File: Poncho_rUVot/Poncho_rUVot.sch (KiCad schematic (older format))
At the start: 20 parts, among them J1 Screw_Terminal_01x03, K1 SANYOU_SRD_Form_C, P1 Conn_01x03, P2 Conn_01x03, P3 Conn_01x04, P4 Conn_01x03, P5 Conn_01x02, P6 Conn_01x02, P7 Conn_01x06, P8 Conn_01x04, P9 Conn_01x08, Q1 BC548, Q2 BC548

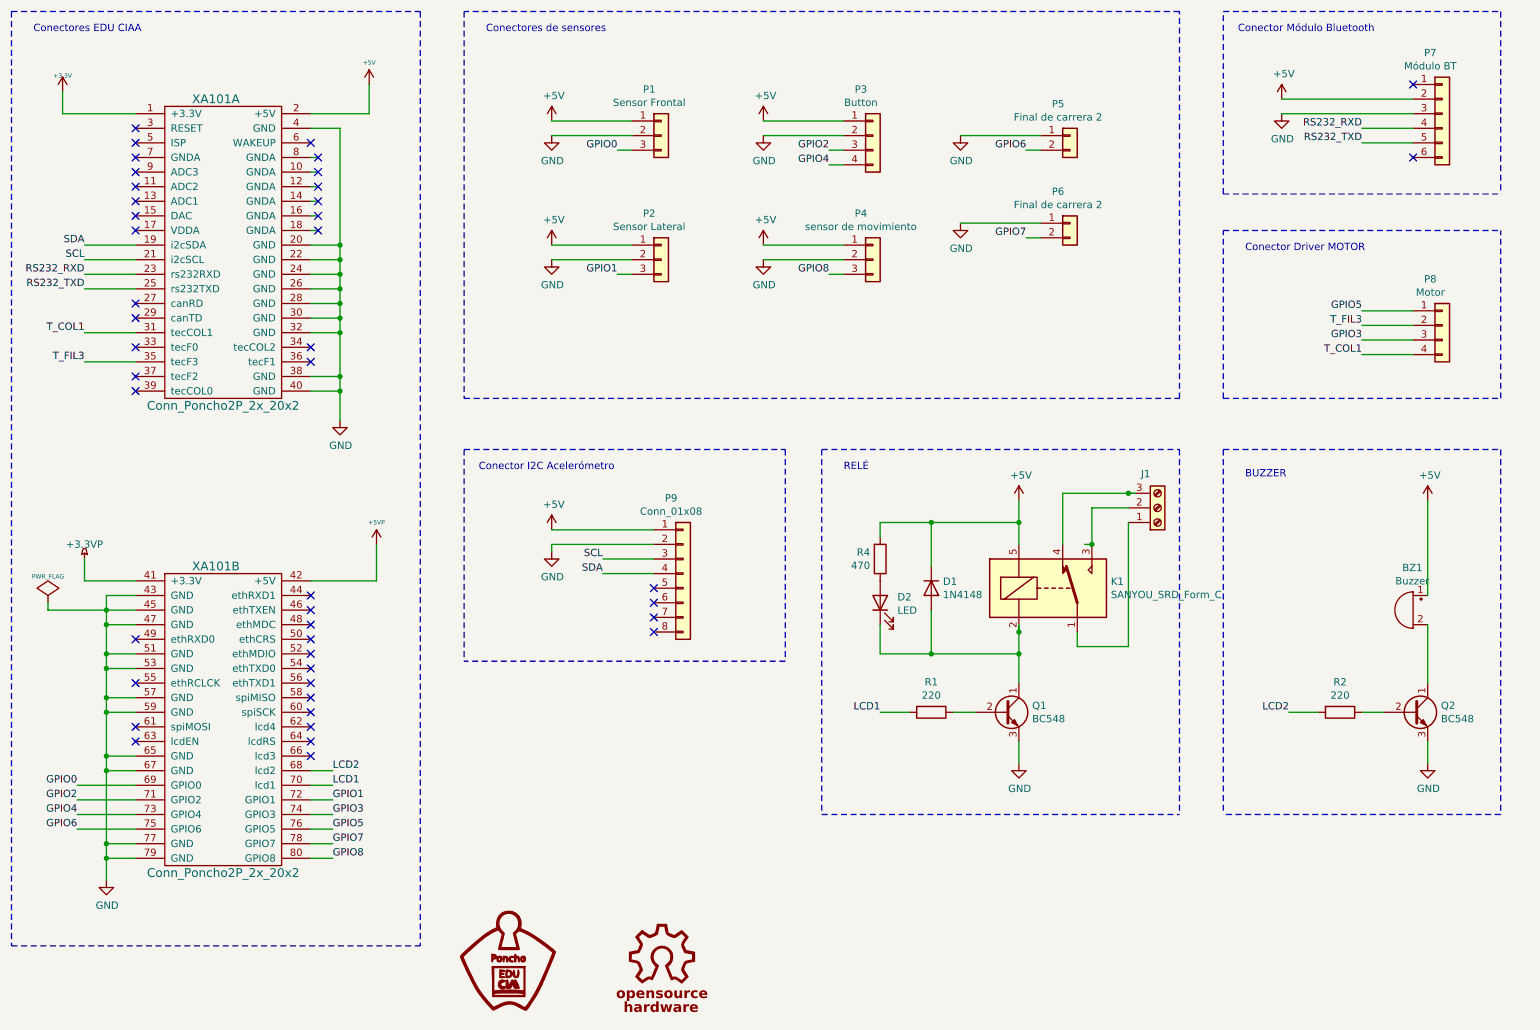
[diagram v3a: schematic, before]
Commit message: Se agrega el PCB
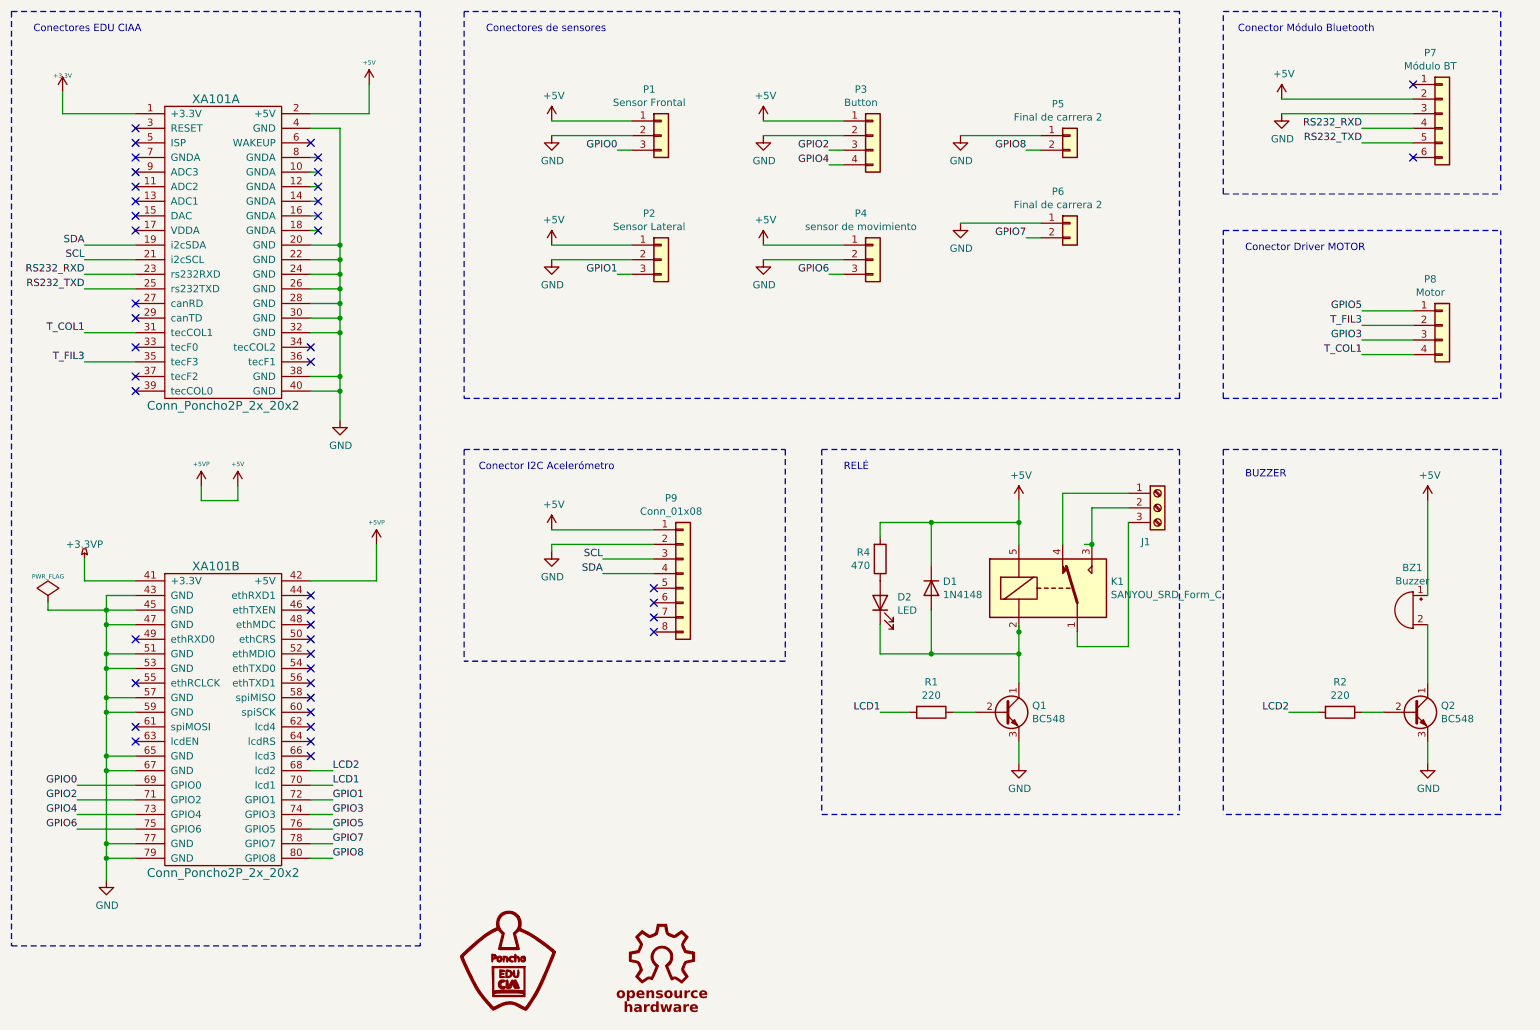
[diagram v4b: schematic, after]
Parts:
- P8: footprint Connector_PinHeader_2.54mm:PinHeader_1x04_P2.54mm_Horizontal -> Connector_PinHeader_2.54mm:PinHeader_1x04_P2.54mm_Vertical
- Q1, Q2: footprint Package_TO_SOT_THT:TO-92_Inline -> Package_TO_SOT_THT:TO-92L
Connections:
- net +5VP is gone; now on net +5V: XA101.42 (+5V)
- net GPIO6: now also P4.3 (Pin_3); no longer P5.2 (Pin_2)
- net GPIO8: now also P5.2 (Pin_2); no longer P4.3 (Pin_3)
- net at J1.1 (Pin_1): now also K1.4; no longer K1.1
- net at J1.3 (Pin_3): now also K1.1; no longer K1.4
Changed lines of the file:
@@
 F 0 "P8" H 10468 3217 50  0000 C CNN
 F 1 "Conn_01x04" H 10468 3126 50  0001 C CNN
-F 2 "Connector_PinHeader_2.54mm:PinHeader_1x04_P2.54mm_Horizontal" H 10550 2900 50  0001 C CNN
+F 2 "Connector_PinHeader_2.54mm:PinHeader_1x04_P2.54mm_Vertical" H 10550 2900 50  0001 C CNN
 F 3 "~" H 10550 2900 50  0001 C CNN
 F 4 "Motor" H 10468 3126 50  0000 C CNN "Field4"
@@
 F 0 "Q2" H 10541 5596 50  0000 L CNN
 F 1 "BC548" H 10541 5505 50  0000 L CNN
-F 2 "Package_TO_SOT_THT:TO-92_Inline" H 10550 5475 50  0001 L CIN
+F 2 "Package_TO_SOT_THT:TO-92L" H 10550 5475 50  0001 L CIN
 F 3 "https://www.onsemi.com/pub/Collateral/BC550-D.pdf" H 10350 5550 50  0001 L CNN
 	1    10350 5550
@@
 Conector Driver MOTOR
 $Comp
-L Poncho_rUVot-rescue:Screw_Terminal_01x03-Connector-conectores-rescue J1
-U 1 1 606412BA
-P 8600 4150
-F 0 "J1" H 8518 3917 50  0000 C CNN
-F 1 "Screw_Terminal_01x03" H 8518 3916 50  0001 C CNN
-F 2 "TerminalBlock_Phoenix:TerminalBlock_Phoenix_MKDS-1,5-3-5.08_1x03_P5.08mm_Horizontal" H 8600 4150 50  0001 C CNN
-F 3 "~" H 8600 4150 50  0001 C CNN
-	1    8600 4150
-	1    0    0    1
-$EndComp
-Wire Wire Line
-	7950 4050 8400 4050
-Connection ~ 8400 4050
-Wire Wire Line
-	8400 4050 8450 4050
-$Comp
 L Poncho_rUVot-rescue:1N4148-Diode-conectores-rescue D1
 U 1 1 60659DD3
@@
 F 0 "Q1" H 7741 5596 50  0000 L CNN
 F 1 "BC548" H 7741 5505 50  0000 L CNN
-F 2 "Package_TO_SOT_THT:TO-92_Inline" H 7750 5475 50  0001 L CIN
+F 2 "Package_TO_SOT_THT:TO-92L" H 7750 5475 50  0001 L CIN
 F 3 "https://www.onsemi.com/pub/Collateral/BC550-D.pdf" H 7550 5550 50  0001 L CNN
 	1    7550 5550
@@
 	5900 2450 6450 2450
 Text Label 6350 2550 2    50   ~ 0
-GPIO8
+GPIO6
 Wire Wire Line
 	6350 2550 6450 2550
@@
 	7700 1700 7800 1700
 Text Label 7700 1700 2    50   ~ 0
-GPIO6
+GPIO8
 $Comp
 L Poncho_rUVot-rescue:Conn_01x03-Connector_Generic-conectores-rescue P1
@@
 EndData
 $EndBitmap
+$Comp
+L Poncho_rUVot-rescue:+5V #PWR0118
+U 1 1 6080CF4B
+P 2300 4000
+F 0 "#PWR0118" H 2300 4090 20  0001 C CNN
+F 1 "+5V" H 2300 4150 30  0000 C CNN
+F 2 "" H 2300 4000 60  0000 C CNN
+F 3 "" H 2300 4000 60  0000 C CNN
+	1    2300 4000
+	1    0    0    -1
+$EndComp
+$Comp
+L Poncho_rUVot-rescue:+5VP #PWR0119
+U 1 1 608141D3
+P 2050 4000
+F 0 "#PWR0119" H 2050 4090 20  0001 C CNN
+F 1 "+5VP" H 2050 4150 30  0000 C CNN
+F 2 "" H 2050 4000 60  0000 C CNN
+F 3 "" H 2050 4000 60  0000 C CNN
+	1    2050 4000
+	1    0    0    -1
+$EndComp
+Wire Wire Line
+	2050 4000 2050 4100
+Wire Wire Line
+	2050 4100 2300 4100
+Wire Wire Line
+	2300 4100 2300 4000
+$Comp
+L Poncho_rUVot-rescue:Screw_Terminal_01x03-Connector-conectores-rescue J1
+U 1 1 606412BA
+P 8600 4150
+F 0 "J1" H 8518 3917 50  0000 C CNN
+F 1 "Screw_Terminal_01x03" H 8518 3916 50  0001 C CNN
+F 2 "TerminalBlock_Phoenix:TerminalBlock_Phoenix_MKDS-1,5-3-5.08_1x03_P5.08mm_Horizontal" H 8600 4150 50  0001 C CNN
+F 3 "~" H 8600 4150 50  0001 C CNN
+	1    8600 4150
+	1    0    0    -1
+$EndComp
+Wire Wire Line
+	7950 4050 8400 4050
 $EndSCHEMATC

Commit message: Correcciones de detalles
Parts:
- P4: Field4 sensor de movimiento -> Sensor de movimiento
- P5: Field4 Final de carrera 2 -> Final de carrera 1
- P9: Field4 (none) -> Acelerometro
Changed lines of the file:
@@
 P 6650 1600
 F 0 "P3" H 6568 1917 50  0000 C CNN
-F 1 "Conn_01x04" H 6568 1826 50  0001 C CNN
+F 1 "Conn_01x04" H 6568 1826 50  0000 C CNN
 F 2 "Connector_PinHeader_2.54mm:PinHeader_1x04_P2.54mm_Horizontal" H 6650 1600 50  0001 C CNN
 F 3 "~" H 6650 1600 50  0001 C CNN
-F 4 "Button" H 6568 1826 50  0000 C CNN "Field4"
+F 4 "Button" H 6650 1300 50  0000 C CNN "Field4"
 	1    6650 1600
 	1    0    0    -1
@@
 $EndComp
 $Comp
-L Poncho_rUVot-rescue:Conn_01x02-Connector_Generic-conectores-rescue P6
-U 1 1 6045EFA2
-P 8000 2200
-F 0 "P6" H 7918 2417 50  0000 C CNN
-F 1 "Conn_01x02" H 7918 2326 50  0001 C CNN
-F 2 "Connector_PinHeader_2.54mm:PinHeader_1x02_P2.54mm_Horizontal" H 8000 2200 50  0001 C CNN
-F 3 "~" H 8000 2200 50  0001 C CNN
-F 4 "Final de carrera 2" H 7918 2326 50  0000 C CNN "Field4"
-	1    8000 2200
-	1    0    0    -1
-$EndComp
-$Comp
 L Poncho_rUVot-rescue:Conn_01x03-Connector_Generic-conectores-rescue P4
 U 1 1 60461281
 P 6650 2450
 F 0 "P4" H 6568 2767 50  0000 C CNN
-F 1 "Conn_01x03" H 6568 2676 50  0001 C CNN
+F 1 "Conn_01x03" H 6568 2676 50  0000 C CNN
 F 2 "Connector_PinHeader_2.54mm:PinHeader_1x03_P2.54mm_Horizontal" H 6650 2450 50  0001 C CNN
 F 3 "~" H 6650 2450 50  0001 C CNN
-F 4 "sensor de movimiento" H 6568 2676 50  0000 C CNN "Field4"
+F 4 "Sensor de movimiento" H 6650 2250 50  0000 C CNN "Field4"
 	1    6650 2450
 	1    0    0    -1
@@
 P 10550 2900
 F 0 "P8" H 10468 3217 50  0000 C CNN
-F 1 "Conn_01x04" H 10468 3126 50  0001 C CNN
+F 1 "Conn_01x04" H 10468 3126 50  0000 C CNN
 F 2 "Connector_PinHeader_2.54mm:PinHeader_1x04_P2.54mm_Vertical" H 10550 2900 50  0001 C CNN
 F 3 "~" H 10550 2900 50  0001 C CNN
-F 4 "Motor" H 10468 3126 50  0000 C CNN "Field4"
+F 4 "Motor" H 10550 2600 50  0000 C CNN "Field4"
 	1    10550 2900
 	1    0    0    -1
@@
 U 1 1 604E6A0D
 P 10350 4850
-F 0 "BZ1" H 10355 5140 50  0000 C CNN
-F 1 "Buzzer" H 10355 5049 50  0000 C CNN
+F 0 "BZ1" H 10400 5150 50  0000 C CNN
+F 1 "Buzzer" H 10400 5050 50  0000 C CNN
 F 2 "Buzzer_Beeper:Buzzer_12x9.5RM7.6" V 10325 4950 50  0001 C CNN
-F 3 "~" V 10325 4950 50  0001 C CNN
+F 3 "http://www.electronicoscaldas.com/datasheet/LTE12-Series.pdf" V 10325 4950 50  0001 C CNN
 	1    10350 4850
 	-1   0    0    -1
@@
 P 10550 1450
 F 0 "P7" H 10468 1867 50  0000 C CNN
-F 1 "Conn_01x06" H 10468 1776 50  0001 C CNN
+F 1 "Conn_01x06" H 10468 1776 50  0000 C CNN
 F 2 "Connector_PinSocket_2.54mm:PinSocket_1x06_P2.54mm_Vertical" H 10550 1450 50  0001 C CNN
 F 3 "~" H 10550 1450 50  0001 C CNN
-F 4 "Módulo BT" H 10468 1776 50  0000 C CNN "Field4"
+F 4 "Módulo BT" H 10500 1050 50  0000 C CNN "Field4"
 	1    10550 1450
 	1    0    0    -1
@@
 F 2 "Connector_PinSocket_2.54mm:PinSocket_1x08_P2.54mm_Vertical" H 5350 4600 50  0001 C CNN
 F 3 "~" H 5350 4600 50  0001 C CNN
+F 4 "Acelerometro" H 5300 4100 50  0000 C CNN "Field4"
 	1    5350 4600
 	1    0    0    -1
@@
 P 8000 1600
 F 0 "P5" H 7918 1817 50  0000 C CNN
-F 1 "Conn_01x02" H 7918 1726 50  0001 C CNN
+F 1 "Conn_01x02" H 7918 1726 50  0000 C CNN
 F 2 "Connector_PinHeader_2.54mm:PinHeader_1x02_P2.54mm_Horizontal" H 8000 1600 50  0001 C CNN
 F 3 "~" H 8000 1600 50  0001 C CNN
-F 4 "Final de carrera 2" H 7918 1726 50  0000 C CNN "Field4"
+F 4 "Final de carrera 1" H 7900 1400 50  0000 C CNN "Field4"
 	1    8000 1600
 	1    0    0    -1
@@
 P 5200 1600
 F 0 "P1" H 5118 1917 50  0000 C CNN
-F 1 "Conn_01x03" H 5118 1826 50  0001 C CNN
+F 1 "Conn_01x03" H 5118 1826 50  0000 C CNN
 F 2 "Connector_PinHeader_2.54mm:PinHeader_1x03_P2.54mm_Horizontal" H 5200 1600 50  0001 C CNN
 F 3 "~" H 5200 1600 50  0001 C CNN
-F 4 "Sensor Frontal" H 5118 1826 50  0000 C CNN "Field4"
+F 4 "Sensor Frontal" H 5150 1400 50  0000 C CNN "Field4"
 	1    5200 1600
 	1    0    0    -1
@@
 P 5200 2450
 F 0 "P2" H 5118 2767 50  0000 C CNN
-F 1 "Conn_01x03" H 5118 2676 50  0001 C CNN
+F 1 "Conn_01x03" H 5118 2676 50  0000 C CNN
 F 2 "Connector_PinHeader_2.54mm:PinHeader_1x03_P2.54mm_Horizontal" H 5200 2450 50  0001 C CNN
 F 3 "~" H 5200 2450 50  0001 C CNN
-F 4 "Sensor Lateral" H 5118 2676 50  0000 C CNN "Field4"
+F 4 "Sensor Lateral" H 5150 2250 50  0000 C CNN "Field4"
 	1    5200 2450
 	1    0    0    -1
@@
 P 8600 4150
 F 0 "J1" H 8518 3917 50  0000 C CNN
-F 1 "Screw_Terminal_01x03" H 8518 3916 50  0001 C CNN
+F 1 "Screw_Terminal_01x03" H 8300 4350 50  0000 C CNN
 F 2 "TerminalBlock_Phoenix:TerminalBlock_Phoenix_MKDS-1,5-3-5.08_1x03_P5.08mm_Horizontal" H 8600 4150 50  0001 C CNN
 F 3 "~" H 8600 4150 50  0001 C CNN
+F 4 "" H 8600 4150 50  0001 C CNN "Field4"
 	1    8600 4150
 	1    0    0    -1
@@
 Wire Wire Line
 	7950 4050 8400 4050
+$Comp
+L Poncho_rUVot-rescue:Conn_01x02-Connector_Generic-conectores-rescue P6
+U 1 1 6045EFA2
+P 8000 2200
+F 0 "P6" H 7918 2417 50  0000 C CNN
+F 1 "Conn_01x02" H 7918 2326 50  0000 C CNN
+F 2 "Connector_PinHeader_2.54mm:PinHeader_1x02_P2.54mm_Horizontal" H 8000 2200 50  0001 C CNN
+F 3 "~" H 8000 2200 50  0001 C CNN
+F 4 "Final de carrera 2" H 7900 2000 50  0000 C CNN "Field4"
+	1    8000 2200
+	1    0    0    -1
+$EndComp
 $EndSCHEMATC
